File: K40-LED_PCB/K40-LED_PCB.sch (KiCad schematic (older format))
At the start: 14 parts, among them p1 12V_Pad

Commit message: PCb_Complete
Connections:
- net labels removed: GND
- wire segments 24 -> 23
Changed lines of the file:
@@
 	5250 5250 5750 5250
-$Comp
-L power:GND #PWR0101
-U 1 1 60E0B72B
-P 5250 5400
-F 0 "#PWR0101" H 5250 5150 50  0001 C CNN
-F 1 "GND" H 5255 5227 50  0000 C CNN
-F 2 "" H 5250 5400 50  0001 C CNN
-F 3 "" H 5250 5400 50  0001 C CNN
-	1    5250 5400
-	1    0    0    -1
-$EndComp
-Wire Wire Line
-	5250 5400 5250 5250
 $Comp
 L 12V_PAD_Symb:12V_Pad p1
@@
 	5250 2450 5750 2450
 Wire Wire Line
-	6900 3200 6900 5250
-Wire Wire Line
 	6900 5250 5750 5250
 Connection ~ 5750 5250
+Wire Wire Line
+	6900 3175 6900 5250
 $EndSCHEMATC

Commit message: Connect  symbol to new footprint
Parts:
- D1, D10, D11, D12, D2, D3, D4, D5, D6, D7, D8, D9: footprint LRST-C190KGKT:LEDC1608X35N -> SPMWH1228FD5WATUS3_FOOTPRINT:LED_SPMWH1228FD5WARMSE
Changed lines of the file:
@@
 F 0 "D4" H 4700 3831 50  0000 C CNN
 F 1 "LTST-C190KGKT" H 4700 3740 50  0000 C CNN
-F 2 "LRST-C190KGKT:LEDC1608X35N" H 4750 3500 50  0001 L BNN
+F 2 "SPMWH1228FD5WATUS3_FOOTPRINT:LED_SPMWH1228FD5WARMSE" H 4750 3500 50  0001 L BNN
 F 3 "" H 4750 3500 50  0001 L BNN
 	1    4750 3500
@@
 F 0 "D7" H 4700 4531 50  0000 C CNN
 F 1 "LTST-C190KGKT" H 4700 4440 50  0000 C CNN
-F 2 "LRST-C190KGKT:LEDC1608X35N" H 4750 4200 50  0001 L BNN
+F 2 "SPMWH1228FD5WATUS3_FOOTPRINT:LED_SPMWH1228FD5WARMSE" H 4750 4200 50  0001 L BNN
 F 3 "" H 4750 4200 50  0001 L BNN
 	1    4750 4200
@@
 F 0 "D10" H 4700 5231 50  0000 C CNN
 F 1 "LTST-C190KGKT" H 4700 5140 50  0000 C CNN
-F 2 "LRST-C190KGKT:LEDC1608X35N" H 4750 4900 50  0001 L BNN
+F 2 "SPMWH1228FD5WATUS3_FOOTPRINT:LED_SPMWH1228FD5WARMSE" H 4750 4900 50  0001 L BNN
 F 3 "" H 4750 4900 50  0001 L BNN
 	1    4750 4900
@@
 F 0 "D2" H 5200 3131 50  0000 C CNN
 F 1 "LTST-C190KGKT" H 5200 3040 50  0000 C CNN
-F 2 "LRST-C190KGKT:LEDC1608X35N" H 5250 2800 50  0001 L BNN
+F 2 "SPMWH1228FD5WATUS3_FOOTPRINT:LED_SPMWH1228FD5WARMSE" H 5250 2800 50  0001 L BNN
 F 3 "" H 5250 2800 50  0001 L BNN
 	1    5250 2800
@@
 F 0 "D5" H 5200 3831 50  0000 C CNN
 F 1 "LTST-C190KGKT" H 5200 3740 50  0000 C CNN
-F 2 "LRST-C190KGKT:LEDC1608X35N" H 5250 3500 50  0001 L BNN
+F 2 "SPMWH1228FD5WATUS3_FOOTPRINT:LED_SPMWH1228FD5WARMSE" H 5250 3500 50  0001 L BNN
 F 3 "" H 5250 3500 50  0001 L BNN
 	1    5250 3500
@@
 F 0 "D8" H 5200 4531 50  0000 C CNN
 F 1 "LTST-C190KGKT" H 5200 4440 50  0000 C CNN
-F 2 "LRST-C190KGKT:LEDC1608X35N" H 5250 4200 50  0001 L BNN
+F 2 "SPMWH1228FD5WATUS3_FOOTPRINT:LED_SPMWH1228FD5WARMSE" H 5250 4200 50  0001 L BNN
 F 3 "" H 5250 4200 50  0001 L BNN
 	1    5250 4200
@@
 F 0 "D11" H 5200 5231 50  0000 C CNN
 F 1 "LTST-C190KGKT" H 5200 5140 50  0000 C CNN
-F 2 "LRST-C190KGKT:LEDC1608X35N" H 5250 4900 50  0001 L BNN
+F 2 "SPMWH1228FD5WATUS3_FOOTPRINT:LED_SPMWH1228FD5WARMSE" H 5250 4900 50  0001 L BNN
 F 3 "" H 5250 4900 50  0001 L BNN
 	1    5250 4900
@@
 F 0 "D3" H 5700 3131 50  0000 C CNN
 F 1 "LTST-C190KGKT" H 5700 3040 50  0000 C CNN
-F 2 "LRST-C190KGKT:LEDC1608X35N" H 5750 2800 50  0001 L BNN
+F 2 "SPMWH1228FD5WATUS3_FOOTPRINT:LED_SPMWH1228FD5WARMSE" H 5750 2800 50  0001 L BNN
 F 3 "" H 5750 2800 50  0001 L BNN
 	1    5750 2800
@@
 F 0 "D6" H 5700 3831 50  0000 C CNN
 F 1 "LTST-C190KGKT" H 5700 3740 50  0000 C CNN
-F 2 "LRST-C190KGKT:LEDC1608X35N" H 5750 3500 50  0001 L BNN
+F 2 "SPMWH1228FD5WATUS3_FOOTPRINT:LED_SPMWH1228FD5WARMSE" H 5750 3500 50  0001 L BNN
 F 3 "" H 5750 3500 50  0001 L BNN
 	1    5750 3500
@@
 F 0 "D9" H 5700 4531 50  0000 C CNN
 F 1 "LTST-C190KGKT" H 5700 4440 50  0000 C CNN
-F 2 "LRST-C190KGKT:LEDC1608X35N" H 5750 4200 50  0001 L BNN
+F 2 "SPMWH1228FD5WATUS3_FOOTPRINT:LED_SPMWH1228FD5WARMSE" H 5750 4200 50  0001 L BNN
 F 3 "" H 5750 4200 50  0001 L BNN
 	1    5750 4200
@@
 F 0 "D12" H 5700 5231 50  0000 C CNN
 F 1 "LTST-C190KGKT" H 5700 5140 50  0000 C CNN
-F 2 "LRST-C190KGKT:LEDC1608X35N" H 5750 4900 50  0001 L BNN
+F 2 "SPMWH1228FD5WATUS3_FOOTPRINT:LED_SPMWH1228FD5WARMSE" H 5750 4900 50  0001 L BNN
 F 3 "" H 5750 4900 50  0001 L BNN
 	1    5750 4900
@@
 F 0 "D1" H 4700 3131 50  0000 C CNN
 F 1 "LTST-C190KGKT" H 4700 3040 50  0000 C CNN
-F 2 "LRST-C190KGKT:LEDC1608X35N" H 4750 2800 50  0001 L BNN
+F 2 "SPMWH1228FD5WATUS3_FOOTPRINT:LED_SPMWH1228FD5WARMSE" H 4750 2800 50  0001 L BNN
 F 3 "" H 4750 2800 50  0001 L BNN
 	1    4750 2800

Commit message: Symbol Changes
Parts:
- R1: value 200 -> 18
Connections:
- net at D1.A, D2.A, D3.A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: now also D10.A
- net at D7.C: now also D12.C, D8.C, D9.C, p1.1 (GND); no longer D10.A
- net at D11.A: now also D10.C; no longer D8.C
- net at D12.A: now also D11.C; no longer D9.C
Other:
- moved on the sheet: D10, D11, D12
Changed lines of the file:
@@
 L LTST-C190KGKT:LTST-C190KGKT D10
 U 1 1 60DFDC8B
-P 4750 4900
-F 0 "D10" H 4700 5231 50  0000 C CNN
-F 1 "LTST-C190KGKT" H 4700 5140 50  0000 C CNN
-F 2 "SPMWH1228FD5WATUS3_FOOTPRINT:LED_SPMWH1228FD5WARMSE" H 4750 4900 50  0001 L BNN
-F 3 "" H 4750 4900 50  0001 L BNN
-	1    4750 4900
+P 6250 2800
+F 0 "D10" H 6200 3131 50  0000 C CNN
+F 1 "LTST-C190KGKT" H 6200 3040 50  0000 C CNN
+F 2 "SPMWH1228FD5WATUS3_FOOTPRINT:LED_SPMWH1228FD5WARMSE" H 6250 2800 50  0001 L BNN
+F 3 "" H 6250 2800 50  0001 L BNN
+	1    6250 2800
 	0    1    1    0
 $EndComp
@@
 L LTST-C190KGKT:LTST-C190KGKT D11
 U 1 1 60E0569B
-P 5250 4900
-F 0 "D11" H 5200 5231 50  0000 C CNN
-F 1 "LTST-C190KGKT" H 5200 5140 50  0000 C CNN
-F 2 "SPMWH1228FD5WATUS3_FOOTPRINT:LED_SPMWH1228FD5WARMSE" H 5250 4900 50  0001 L BNN
-F 3 "" H 5250 4900 50  0001 L BNN
-	1    5250 4900
+P 6250 3500
+F 0 "D11" H 6200 3831 50  0000 C CNN
+F 1 "LTST-C190KGKT" H 6200 3740 50  0000 C CNN
+F 2 "SPMWH1228FD5WATUS3_FOOTPRINT:LED_SPMWH1228FD5WARMSE" H 6250 3500 50  0001 L BNN
+F 3 "" H 6250 3500 50  0001 L BNN
+	1    6250 3500
 	0    1    1    0
 $EndComp
@@
 L LTST-C190KGKT:LTST-C190KGKT D12
 U 1 1 60E07BD9
-P 5750 4900
-F 0 "D12" H 5700 5231 50  0000 C CNN
-F 1 "LTST-C190KGKT" H 5700 5140 50  0000 C CNN
-F 2 "SPMWH1228FD5WATUS3_FOOTPRINT:LED_SPMWH1228FD5WARMSE" H 5750 4900 50  0001 L BNN
-F 3 "" H 5750 4900 50  0001 L BNN
-	1    5750 4900
-	0    1    1    0
-$EndComp
-$Comp
-L LTST-C190KGKT:LTST-C190KGKT D1
-U 1 1 60DF68F4
-P 4750 2800
-F 0 "D1" H 4700 3131 50  0000 C CNN
-F 1 "LTST-C190KGKT" H 4700 3040 50  0000 C CNN
-F 2 "SPMWH1228FD5WATUS3_FOOTPRINT:LED_SPMWH1228FD5WARMSE" H 4750 2800 50  0001 L BNN
-F 3 "" H 4750 2800 50  0001 L BNN
-	1    4750 2800
+P 6250 4200
+F 0 "D12" H 6200 4531 50  0000 C CNN
+F 1 "LTST-C190KGKT" H 6200 4440 50  0000 C CNN
+F 2 "SPMWH1228FD5WATUS3_FOOTPRINT:LED_SPMWH1228FD5WARMSE" H 6250 4200 50  0001 L BNN
+F 3 "" H 6250 4200 50  0001 L BNN
+	1    6250 4200
 	0    1    1    0
 $EndComp
@@
 	4750 3700 4750 3900
 Wire Wire Line
-	4750 4400 4750 4600
-Wire Wire Line
 	5250 3000 5250 3200
 Wire Wire Line
 	5250 3700 5250 3900
 Wire Wire Line
-	5250 4400 5250 4600
-Wire Wire Line
 	5750 3000 5750 3200
 Wire Wire Line
 	5750 3700 5750 3900
-Wire Wire Line
-	5750 4400 5750 4600
-Wire Wire Line
-	4750 5100 4750 5250
-Wire Wire Line
-	4750 5250 5250 5250
-Wire Wire Line
-	5750 5250 5750 5100
-Wire Wire Line
-	5250 5100 5250 5250
-Connection ~ 5250 5250
-Wire Wire Line
-	5250 5250 5750 5250
 $Comp
 L 12V_PAD_Symb:12V_Pad p1
@@
 P 6900 2550
 F 0 "R1" H 6841 2504 50  0000 R CNN
-F 1 "200" H 6841 2595 50  0000 R CNN
+F 1 "18" H 6841 2595 50  0000 R CNN
 F 2 "Resistor_SMD:R_0805_2012Metric" H 6900 2550 50  0001 C CNN
 F 3 "~" H 6900 2550 50  0001 C CNN
@@
 	6900 3025 6900 2650
 Wire Wire Line
-	6900 2450 5750 2450
+	6900 3175 6900 4450
+$Comp
+L LTST-C190KGKT:LTST-C190KGKT D1
+U 1 1 60DF68F4
+P 4750 2800
+F 0 "D1" H 4700 3131 50  0000 C CNN
+F 1 "LTST-C190KGKT" H 4700 3040 50  0000 C CNN
+F 2 "SPMWH1228FD5WATUS3_FOOTPRINT:LED_SPMWH1228FD5WARMSE" H 4750 2800 50  0001 L BNN
+F 3 "" H 4750 2800 50  0001 L BNN
+	1    4750 2800
+	0    1    1    0
+$EndComp
+Wire Wire Line
+	6250 3000 6250 3200
+Wire Wire Line
+	6250 3700 6250 3900
+Wire Wire Line
+	6900 2450 6250 2450
+Wire Wire Line
+	6250 2450 6250 2500
+Wire Wire Line
+	6250 2450 5750 2450
 Wire Wire Line
 	5750 2450 5750 2500
+Connection ~ 6250 2450
+Wire Wire Line
+	5750 2450 5250 2450
 Wire Wire Line
 	5250 2450 5250 2500
 Connection ~ 5750 2450
 Wire Wire Line
+	5250 2450 4750 2450
+Wire Wire Line
 	4750 2450 4750 2500
-Wire Wire Line
-	4750 2450 5250 2450
 Connection ~ 5250 2450
 Wire Wire Line
-	5250 2450 5750 2450
+	4750 4400 4750 4450
 Wire Wire Line
-	6900 5250 5750 5250
-Connection ~ 5750 5250
+	4750 4450 5250 4450
 Wire Wire Line
-	6900 3175 6900 5250
+	5250 4450 5250 4400
+Wire Wire Line
+	5250 4450 5750 4450
+Wire Wire Line
+	5750 4450 5750 4400
+Connection ~ 5250 4450
+Wire Wire Line
+	5750 4450 6250 4450
+Wire Wire Line
+	6250 4450 6250 4400
+Connection ~ 5750 4450
+Wire Wire Line
+	6250 4450 6900 4450
+Connection ~ 6250 4450
 $EndSCHEMATC

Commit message: More Footprint updates
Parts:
- p1: footprint 12V_Pad:12V_Supply_Pad -> 12V_Through_Hole:12V_Through_Hole
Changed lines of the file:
@@
 F 0 "p1" V 7029 3053 50  0000 L CNN
 F 1 "12V_Pad" V 7120 3053 50  0000 L CNN
-F 2 "12V_Pad:12V_Supply_Pad" H 7075 3100 50  0001 C CNN
+F 2 "12V_Through_Hole:12V_Through_Hole" H 7075 3100 50  0001 C CNN
 F 3 "" H 7075 3100 50  0001 C CNN
 	1    7075 3100

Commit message: Footprint updates
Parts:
- D1, D10, D11, D12, D2, D3, D4, D5, D6, D7, D8, D9: footprint SPMWH1228FD5WATUS3_FOOTPRINT:LED_SPMWH1228FD5WARMSE -> Cree_MX3AWT-A1-R250-000BE3:Cree_MX3AWT-A1-R250-000BE3
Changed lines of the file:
@@
 F 0 "D4" H 4700 3831 50  0000 C CNN
 F 1 "LTST-C190KGKT" H 4700 3740 50  0000 C CNN
-F 2 "SPMWH1228FD5WATUS3_FOOTPRINT:LED_SPMWH1228FD5WARMSE" H 4750 3500 50  0001 L BNN
+F 2 "Cree_MX3AWT-A1-R250-000BE3:Cree_MX3AWT-A1-R250-000BE3" H 4750 3500 50  0001 L BNN
 F 3 "" H 4750 3500 50  0001 L BNN
 	1    4750 3500
@@
 F 0 "D7" H 4700 4531 50  0000 C CNN
 F 1 "LTST-C190KGKT" H 4700 4440 50  0000 C CNN
-F 2 "SPMWH1228FD5WATUS3_FOOTPRINT:LED_SPMWH1228FD5WARMSE" H 4750 4200 50  0001 L BNN
+F 2 "Cree_MX3AWT-A1-R250-000BE3:Cree_MX3AWT-A1-R250-000BE3" H 4750 4200 50  0001 L BNN
 F 3 "" H 4750 4200 50  0001 L BNN
 	1    4750 4200
@@
 F 0 "D10" H 6200 3131 50  0000 C CNN
 F 1 "LTST-C190KGKT" H 6200 3040 50  0000 C CNN
-F 2 "SPMWH1228FD5WATUS3_FOOTPRINT:LED_SPMWH1228FD5WARMSE" H 6250 2800 50  0001 L BNN
+F 2 "Cree_MX3AWT-A1-R250-000BE3:Cree_MX3AWT-A1-R250-000BE3" H 6250 2800 50  0001 L BNN
 F 3 "" H 6250 2800 50  0001 L BNN
 	1    6250 2800
@@
 F 0 "D2" H 5200 3131 50  0000 C CNN
 F 1 "LTST-C190KGKT" H 5200 3040 50  0000 C CNN
-F 2 "SPMWH1228FD5WATUS3_FOOTPRINT:LED_SPMWH1228FD5WARMSE" H 5250 2800 50  0001 L BNN
+F 2 "Cree_MX3AWT-A1-R250-000BE3:Cree_MX3AWT-A1-R250-000BE3" H 5250 2800 50  0001 L BNN
 F 3 "" H 5250 2800 50  0001 L BNN
 	1    5250 2800
@@
 F 0 "D5" H 5200 3831 50  0000 C CNN
 F 1 "LTST-C190KGKT" H 5200 3740 50  0000 C CNN
-F 2 "SPMWH1228FD5WATUS3_FOOTPRINT:LED_SPMWH1228FD5WARMSE" H 5250 3500 50  0001 L BNN
+F 2 "Cree_MX3AWT-A1-R250-000BE3:Cree_MX3AWT-A1-R250-000BE3" H 5250 3500 50  0001 L BNN
 F 3 "" H 5250 3500 50  0001 L BNN
 	1    5250 3500
@@
 F 0 "D8" H 5200 4531 50  0000 C CNN
 F 1 "LTST-C190KGKT" H 5200 4440 50  0000 C CNN
-F 2 "SPMWH1228FD5WATUS3_FOOTPRINT:LED_SPMWH1228FD5WARMSE" H 5250 4200 50  0001 L BNN
+F 2 "Cree_MX3AWT-A1-R250-000BE3:Cree_MX3AWT-A1-R250-000BE3" H 5250 4200 50  0001 L BNN
 F 3 "" H 5250 4200 50  0001 L BNN
 	1    5250 4200
@@
 F 0 "D11" H 6200 3831 50  0000 C CNN
 F 1 "LTST-C190KGKT" H 6200 3740 50  0000 C CNN
-F 2 "SPMWH1228FD5WATUS3_FOOTPRINT:LED_SPMWH1228FD5WARMSE" H 6250 3500 50  0001 L BNN
+F 2 "Cree_MX3AWT-A1-R250-000BE3:Cree_MX3AWT-A1-R250-000BE3" H 6250 3500 50  0001 L BNN
 F 3 "" H 6250 3500 50  0001 L BNN
 	1    6250 3500
@@
 F 0 "D3" H 5700 3131 50  0000 C CNN
 F 1 "LTST-C190KGKT" H 5700 3040 50  0000 C CNN
-F 2 "SPMWH1228FD5WATUS3_FOOTPRINT:LED_SPMWH1228FD5WARMSE" H 5750 2800 50  0001 L BNN
+F 2 "Cree_MX3AWT-A1-R250-000BE3:Cree_MX3AWT-A1-R250-000BE3" H 5750 2800 50  0001 L BNN
 F 3 "" H 5750 2800 50  0001 L BNN
 	1    5750 2800
@@
 F 0 "D6" H 5700 3831 50  0000 C CNN
 F 1 "LTST-C190KGKT" H 5700 3740 50  0000 C CNN
-F 2 "SPMWH1228FD5WATUS3_FOOTPRINT:LED_SPMWH1228FD5WARMSE" H 5750 3500 50  0001 L BNN
+F 2 "Cree_MX3AWT-A1-R250-000BE3:Cree_MX3AWT-A1-R250-000BE3" H 5750 3500 50  0001 L BNN
 F 3 "" H 5750 3500 50  0001 L BNN
 	1    5750 3500
@@
 F 0 "D9" H 5700 4531 50  0000 C CNN
 F 1 "LTST-C190KGKT" H 5700 4440 50  0000 C CNN
-F 2 "SPMWH1228FD5WATUS3_FOOTPRINT:LED_SPMWH1228FD5WARMSE" H 5750 4200 50  0001 L BNN
+F 2 "Cree_MX3AWT-A1-R250-000BE3:Cree_MX3AWT-A1-R250-000BE3" H 5750 4200 50  0001 L BNN
 F 3 "" H 5750 4200 50  0001 L BNN
 	1    5750 4200
@@
 F 0 "D12" H 6200 4531 50  0000 C CNN
 F 1 "LTST-C190KGKT" H 6200 4440 50  0000 C CNN
-F 2 "SPMWH1228FD5WATUS3_FOOTPRINT:LED_SPMWH1228FD5WARMSE" H 6250 4200 50  0001 L BNN
+F 2 "Cree_MX3AWT-A1-R250-000BE3:Cree_MX3AWT-A1-R250-000BE3" H 6250 4200 50  0001 L BNN
 F 3 "" H 6250 4200 50  0001 L BNN
 	1    6250 4200
@@
 F 0 "D1" H 4700 3131 50  0000 C CNN
 F 1 "LTST-C190KGKT" H 4700 3040 50  0000 C CNN
-F 2 "SPMWH1228FD5WATUS3_FOOTPRINT:LED_SPMWH1228FD5WARMSE" H 4750 2800 50  0001 L BNN
+F 2 "Cree_MX3AWT-A1-R250-000BE3:Cree_MX3AWT-A1-R250-000BE3" H 4750 2800 50  0001 L BNN
 F 3 "" H 4750 2800 50  0001 L BNN
 	1    4750 2800

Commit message: Major  PCB  Changes
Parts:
- removed D10, D11, D12, D7, D8, D9: LTST-C190KGKT, Cree_MX3AWT-A1-R250-000BE3:Cree_MX3AWT-A1-R250-000BE3, symbol LTST-C190KGKT:LTST-C190KGKT
- added C? (x4): 0.01uF, symbol Device:C_Small
- added C? (x4): 1uF, symbol Device:C_Small
- added D? (x2): LTST-C190KGKT, LEDC1608X35N, symbol LTST-C190KGKT:LTST-C190KGKT
- added R? (x4): 1, Resistor_SMD:R_0805_2012Metric, symbol Device:R_Small
- added U?: LDD_350HS, symbol LDD-350HS_SYMBOL:LDD_350HS
- added U? (x4): LM3466, symbol LM3466_SYMBOL:LM3466
- R1: value 18 -> 13
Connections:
- net at D1.A, D2.A, D3.A: now also C?.1, C?.1, C?.1, C?.1, D?.A, U?.13 (+Vout_"LED(+)"), U?.14 (+Vout_"LED(+)"), U?.3 (VIN), U?.3 (VIN), U?.3 (VIN), U?.3 (VIN); no longer R1.2
- net at D4.C: now also C?.1, U?.1 (ILED)
- net at D5.C: now also C?.1, U?.1 (ILED)
- net at D6.C: now also C?.1, U?.1 (ILED)
- net at p1.2 (12V): no longer R1.1
- new net: R1.1, U?.23 (+Vin), U?.24 (+Vin)
- new net: U?.1 (-Vin), U?.2 (-Vin)
- new net: U?.2 (COMM), U?.2 (COMM), U?.2 (COMM), U?.2 (COMM)
- new net: U?.4 (VEQ), U?.4 (VEQ), U?.4 (VEQ), U?.4 (VEQ)
- new net: R?.2, U?.6 (SEN), U?.7 (SRC), U?.8 (SRC) (x4)
- new net: D?.A, D?.C
- new net: C?.1, D?.C, U?.1 (ILED)
- new net GND: C?.2, C?.2, C?.2, C?.2, C?.2, C?.2, C?.2, C?.2, R?.1, R?.1, R?.1, R?.1, U?.5 (GND), U?.5 (GND), U?.5 (GND), U?.5 (GND)
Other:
- moved on the sheet: D2, D3, D5, D6, R1, p1

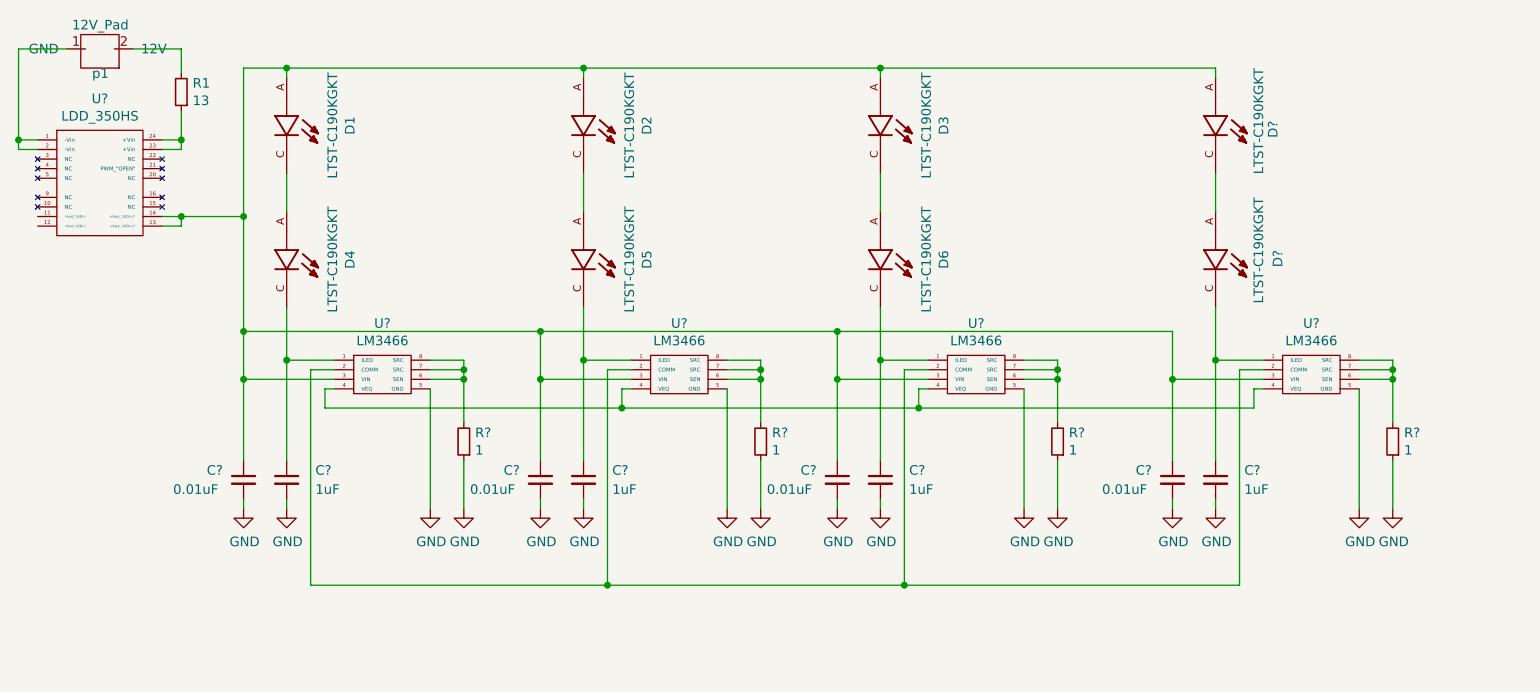
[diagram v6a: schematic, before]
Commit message: PCB_Changes  + footprints
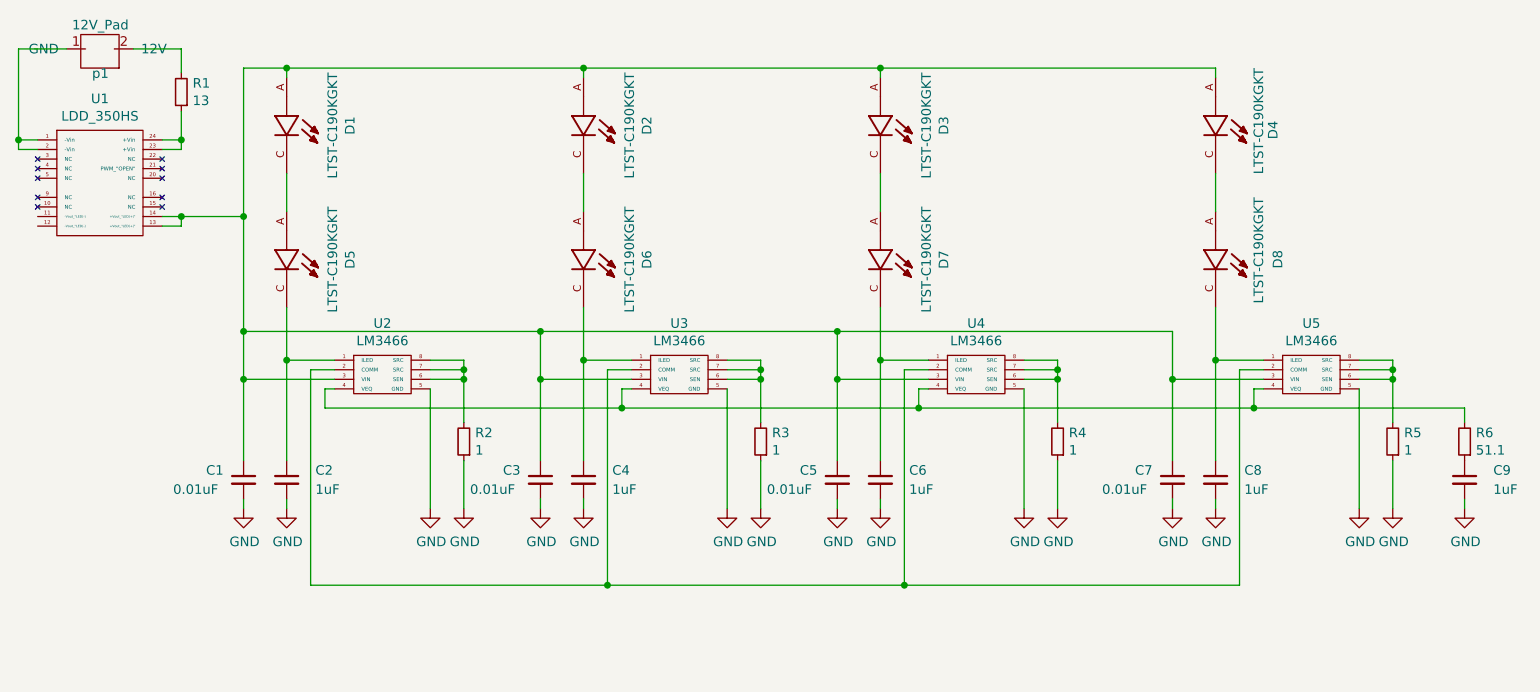
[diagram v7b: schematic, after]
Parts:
- added C9: 1uF, Capacitor_SMD:C_0805_2012Metric, symbol Device:C_Small
- added R6: 51.1, Resistor_SMD:R_0805_2012Metric, symbol Device:R_Small
- C1, C2, C3, C4, C5, C6, C7, C8: renamed from C?; footprint (none) -> Capacitor_SMD:C_0805_2012Metric
- D4, D8: renamed from D?; footprint LEDC1608X35N -> Cree_MX3AWT-A1-R250-000BE3:Cree_MX3AWT-A1-R250-000BE3
- U1: renamed from U?; footprint (none) -> LDD-350HS:LDD-350HS
- U2, U3, U4, U5: renamed from U?; footprint (none) -> LM3466:NOPB
- gave numbers to parts that had none: 4
- renumbered D4 to D5, D5 to D6, D6 to D7
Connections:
- net GND: now also C9.2
- net at U2.4 (VEQ), U3.4 (VEQ), U4.4 (VEQ)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: now also R6.2
- new net: C9.1, R6.1
